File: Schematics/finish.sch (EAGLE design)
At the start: 6 parts, among them U2 TINY85-20-DIP

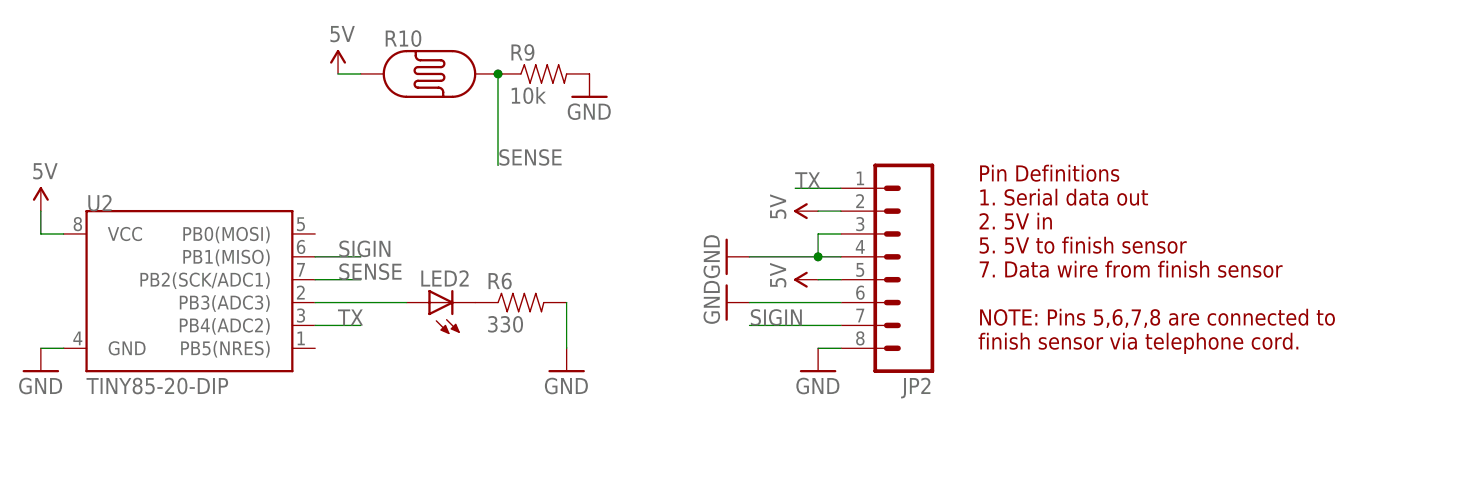
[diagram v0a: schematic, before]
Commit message: Created start sensor schematic.
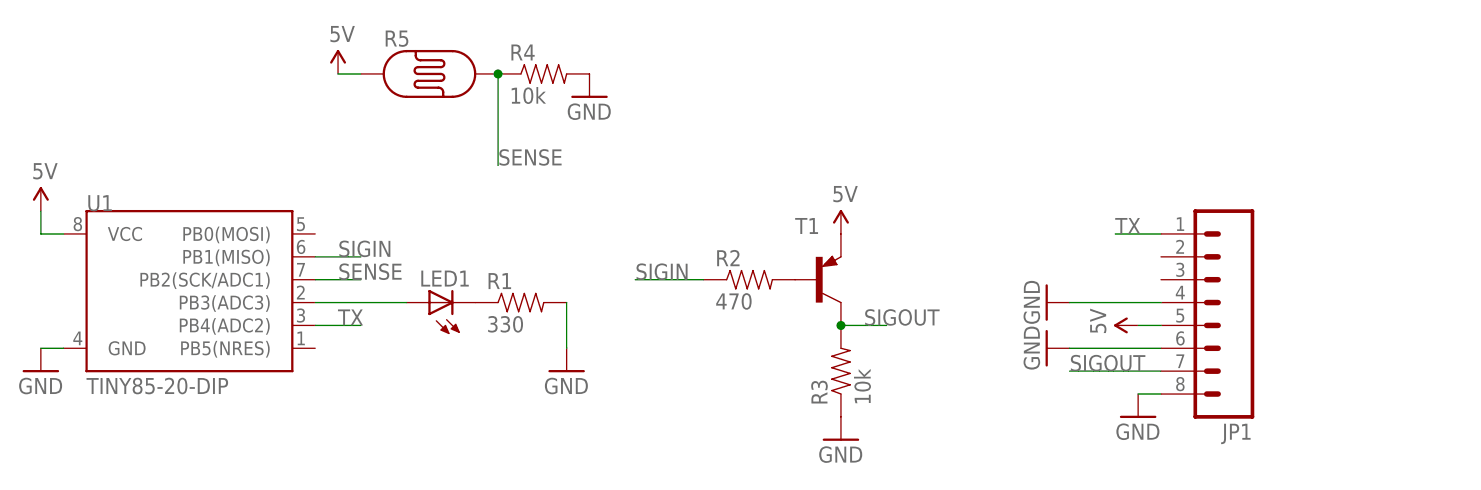
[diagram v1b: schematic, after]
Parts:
- removed JP2: (no value), SparkFun-Connectors:M081X08
- added JP1: (no value), SparkFun-Connectors:M081X08
- added R2: 470, SparkFun-Resistors:RESISTORPTH-1/4W
- added R3: 10k, SparkFun-Resistors:RESISTORPTH-1/4W
- added T1: (no value), transistor-neu-to92:2N3906-PNP-TO92-EBC
- renumbered LED2 to LED1, R10 to R5, R6 to R1, R9 to R4, U2 to U1
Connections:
- new net N$3: R2.2, T1.B
- new net SIGOUT: JP1.7, R3.2, T1.C
- net 5V: now also JP1.5, T1.E; no longer JP2.2, JP2.5
- net GND: now also JP1.4, JP1.6, JP1.8, R3.1; no longer JP2.3, JP2.4, JP2.6, JP2.8
- net SIGIN: now also R2.1; no longer JP2.7
- net TX: now also JP1.1; no longer JP2.1
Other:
- note removed: "Pin Definitions 1. Serial data out 2. 5V in 5. 5V to finish sensor 7. Data wire from finish sensor NOTE: Pins 5,6,7,8 are connected to finish sensor via telephone cord."
